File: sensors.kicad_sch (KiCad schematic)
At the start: 14 parts, among them U3 BMP581, U4 BNO085, Y2 Crystal

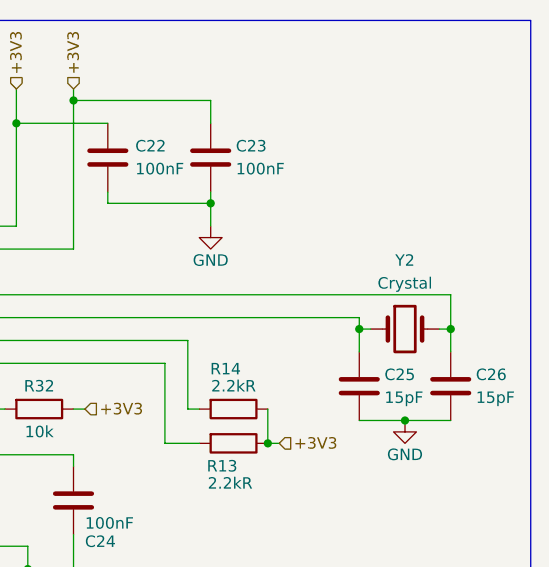
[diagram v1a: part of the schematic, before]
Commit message: Fix foot print for IMU clock
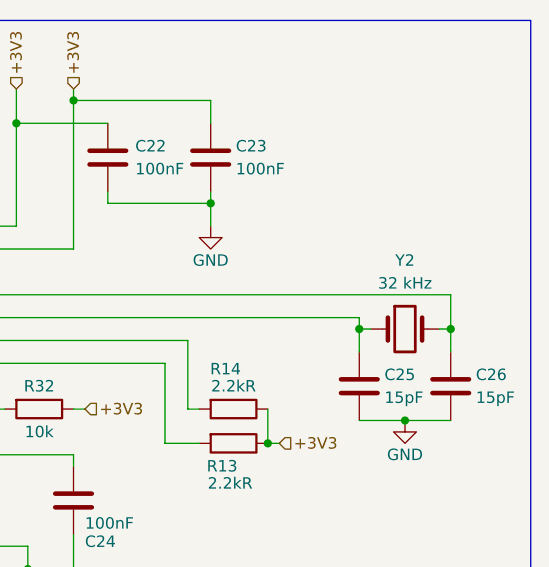
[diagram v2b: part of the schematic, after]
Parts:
- Y2: value Crystal -> 32 kHz; footprint Crystal:Crystal_SMD_0603-2Pin_6.0x3.5mm_HandSoldering -> ABS07_32_768KHZ_T:XTAL_ABS07-32.768KHZ-T
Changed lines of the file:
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@@
 			)
 		)
-		(property "Value" "Crystal"
+		(property "Value" "32 kHz"
 			(at 264.16 92.71 0)
 			(effects
@@
 			)
 		)
-		(property "Footprint" "Crystal:Crystal_SMD_0603-2Pin_6.0x3.5mm_HandSoldering"
+		(property "Footprint" "ABS07_32_768KHZ_T:XTAL_ABS07-32.768KHZ-T"
 			(at 264.16 97.79 0)
 			(effects

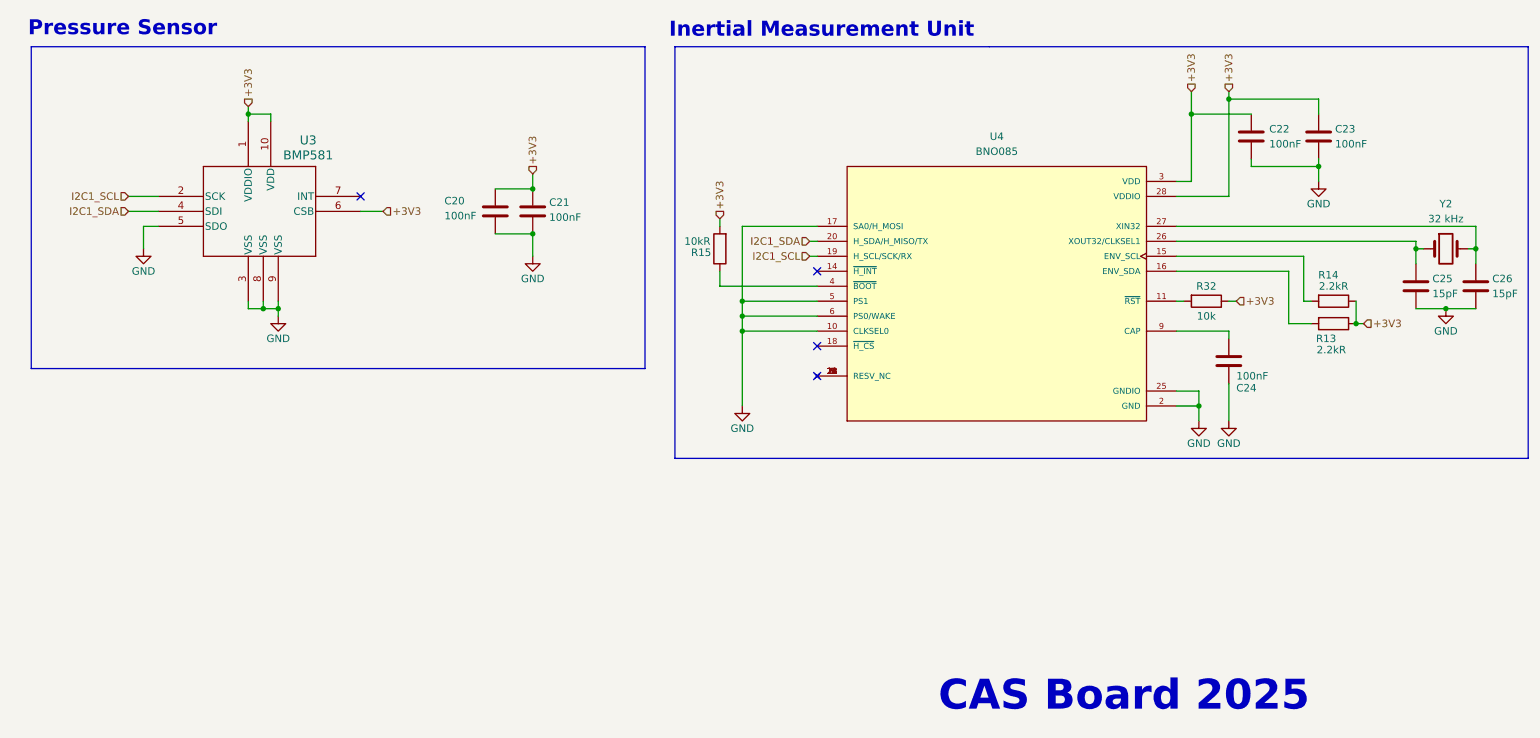
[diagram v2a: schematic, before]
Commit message: Use LCSC parts only
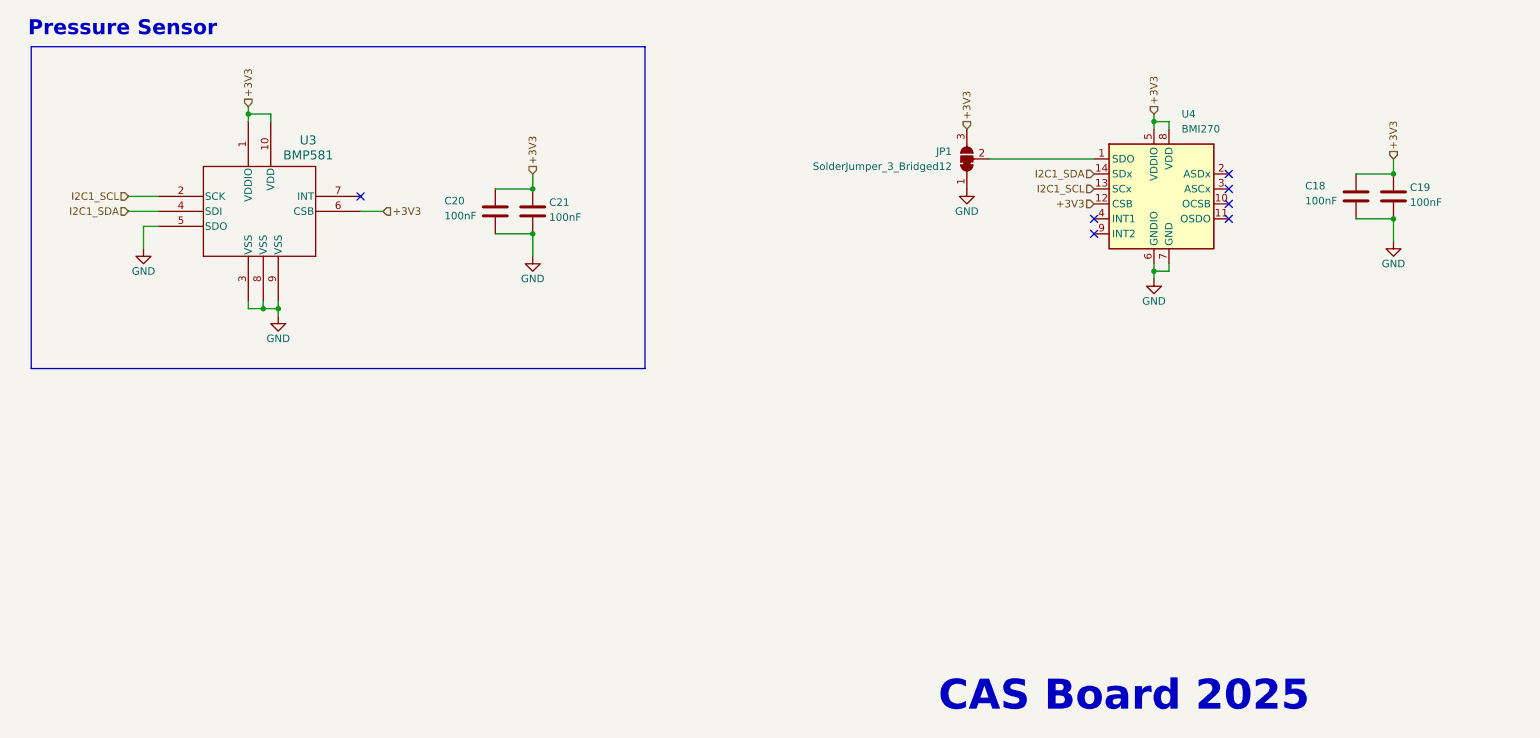
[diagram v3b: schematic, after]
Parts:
- removed C22, C23, C24: 100nF, Capacitor_SMD:C_0805_2012Metric, symbol Device:C
- removed C25, C26: 15pF, Capacitor_SMD:C_0805_2012Metric, symbol Device:C
- removed R13, R14: 2.2kR, Resistor_SMD:R_0805_2012Metric_Pad1.20x1.40mm_HandSolder, symbol Device:R
- removed R15: 10kR, Resistor_SMD:R_0805_2012Metric_Pad1.20x1.40mm_HandSolder, symbol Device:R
- removed R32: 10k, Resistor_SMD:R_0805_2012Metric_Pad1.20x1.40mm_HandSolder, symbol Device:R
- removed U4: BNO085, BNO085:IC_BNO085, symbol BNO085:BNO085
- removed Y2: 32 kHz, ABS07_32_768KHZ_T:XTAL_ABS07-32.768KHZ-T, symbol Device:Crystal
- added C18, C19: 100nF, Capacitor_SMD:C_0805_2012Metric, symbol Device:C
- added JP1: SolderJumper_3_Bridged12, Jumper:SolderJumper-3_P1.3mm_Bridged12_RoundedPad1.0x1.5mm, symbol Jumper:SolderJumper_3_Bridged12
- added U4: BMI270, Package_LGA:Bosch_LGA-14_3x2.5mm_P0.5mm, symbol Sensor_Motion:BMI160
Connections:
- net +3V3: now also C18.1, C19.1, JP1.3 (B), U4.12 (CSB), U4.5 (VDDIO), U4.8 (VDD)
- net GND: now also C18.2, C19.2, JP1.1 (A), U4.6 (GNDIO), U4.7 (GND)
- net I2C1_SCL: now also U4.13 (SCx)
- net I2C1_SDA: now also U4.14 (SDx)
- new net: JP1.2 (C), U4.1 (SDO)
- no-connect marks 4 -> 7
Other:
- note removed: "Inertial Measurement Unit"
